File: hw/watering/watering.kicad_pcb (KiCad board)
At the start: 2 copper layers, 262 x 50 mm, 104 parts, among them J2 USB_C_Receptacle, J3 Conn_01x02_Pin, J4 Conn_01x02_Pin, J6 Conn_01x02_Pin, Q1 2N7002, SW2 KMS221GLFS, SW3 KMS221GLFS, U1 ESP32-C6, U10 MCP6002-xSN, U11 STI3508, U2 DRV8220DSG, U3 W25Q128JVS, U4 STI3508, U5 STI3508, U6 STI3508, U7 NCP163AFCT330T2G, U8 MCP6002-xSN, U9 MCP6002-xSN, Y1 40MHz, Y2 32768Hz

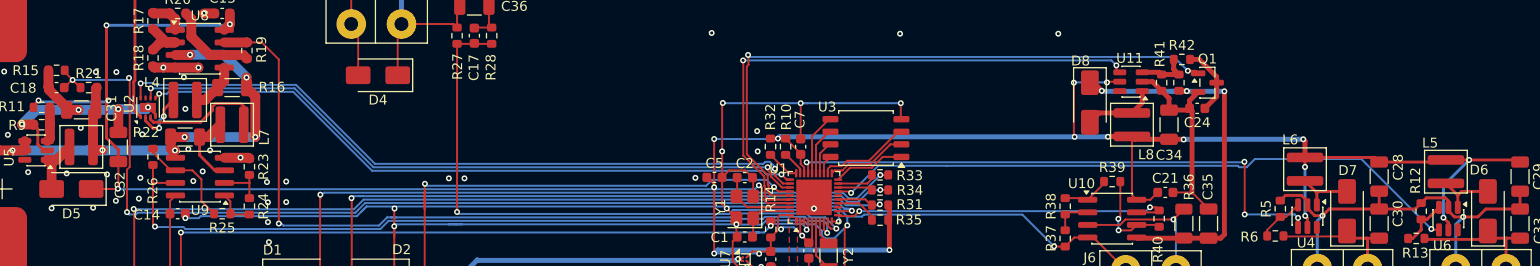
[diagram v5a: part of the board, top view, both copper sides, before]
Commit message: updated inductors
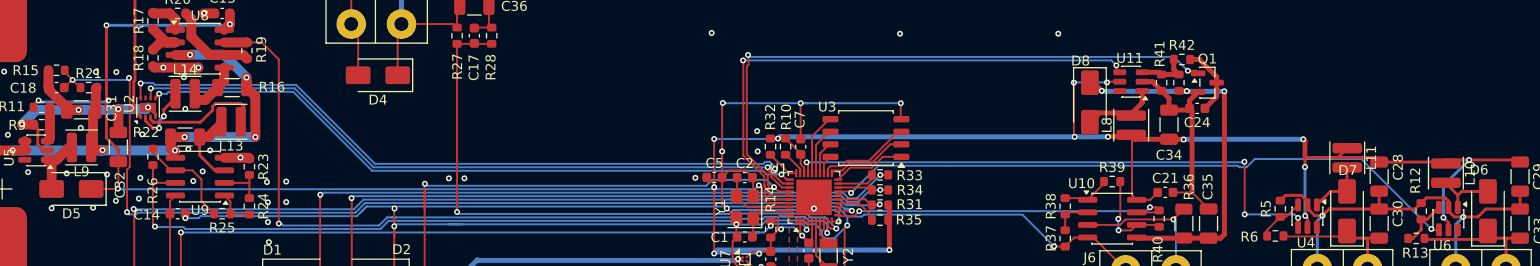
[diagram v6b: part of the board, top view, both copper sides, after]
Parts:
- removed L3, L4, L5, L6, L7: 22u, Inductor_SMD:L_Wuerth_MAPI-4030
- added L10: 22u, Inductor_SMD:L_Changjiang_FTC303020D, F.Cu at (252.0, 127.9)
- added L11: 22u, Inductor_SMD:L_Changjiang_FTC303020D, F.Cu at (242.0, 126.3)
- added L13: 22u, Inductor_SMD:L_Changjiang_FTC303020D, F.Cu at (129.2, 122.7)
- added L14: 22u, Inductor_SMD:L_Changjiang_FTC303020D, F.Cu at (124.5, 119.9)
- added L9: 22u, Inductor_SMD:L_Changjiang_FTC303020D, F.Cu at (114.0, 125.3)
- L8: footprint Inductor_SMD:L_Wuerth_MAPI-4030 -> Inductor_SMD:L_Changjiang_FTC303020D
- moved L8 0.09 mm to (220.2, 123.0)
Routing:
- net /+3V3: track 297.6 -> 299.3 mm

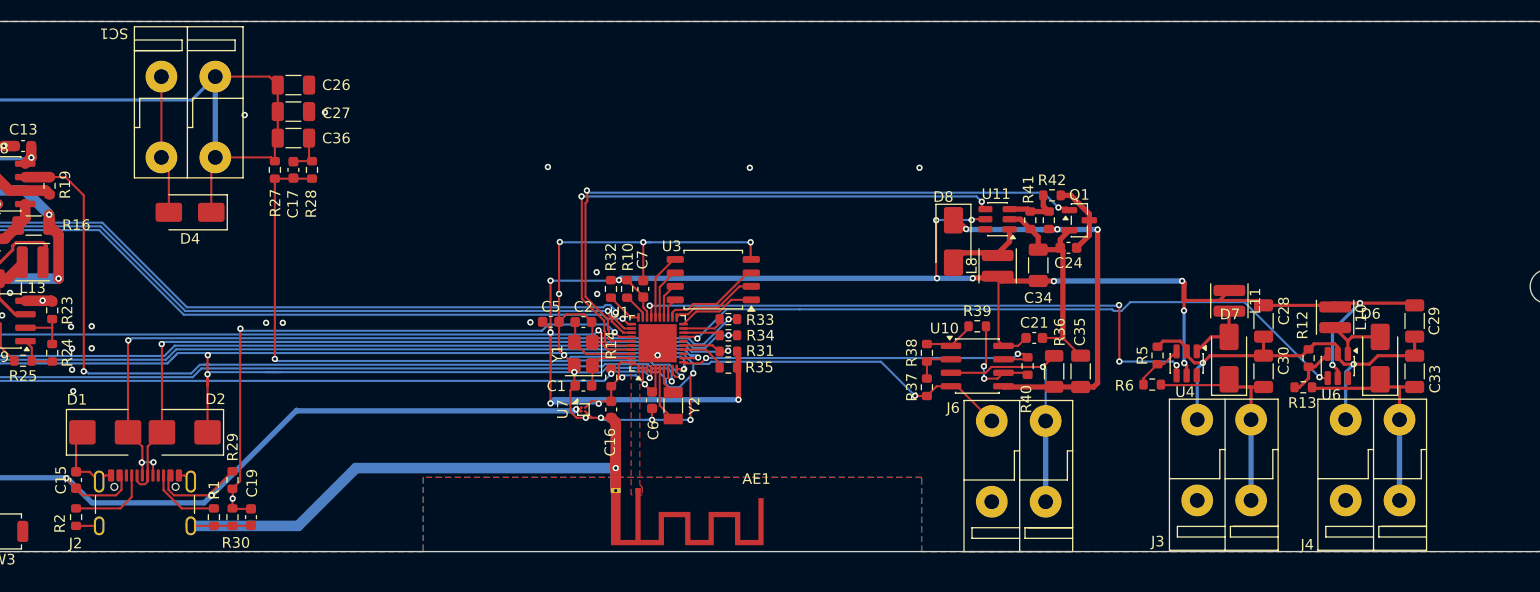
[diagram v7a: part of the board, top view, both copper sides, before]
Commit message: - updated bom - updated dorabo connector footprint - added some stitching vias
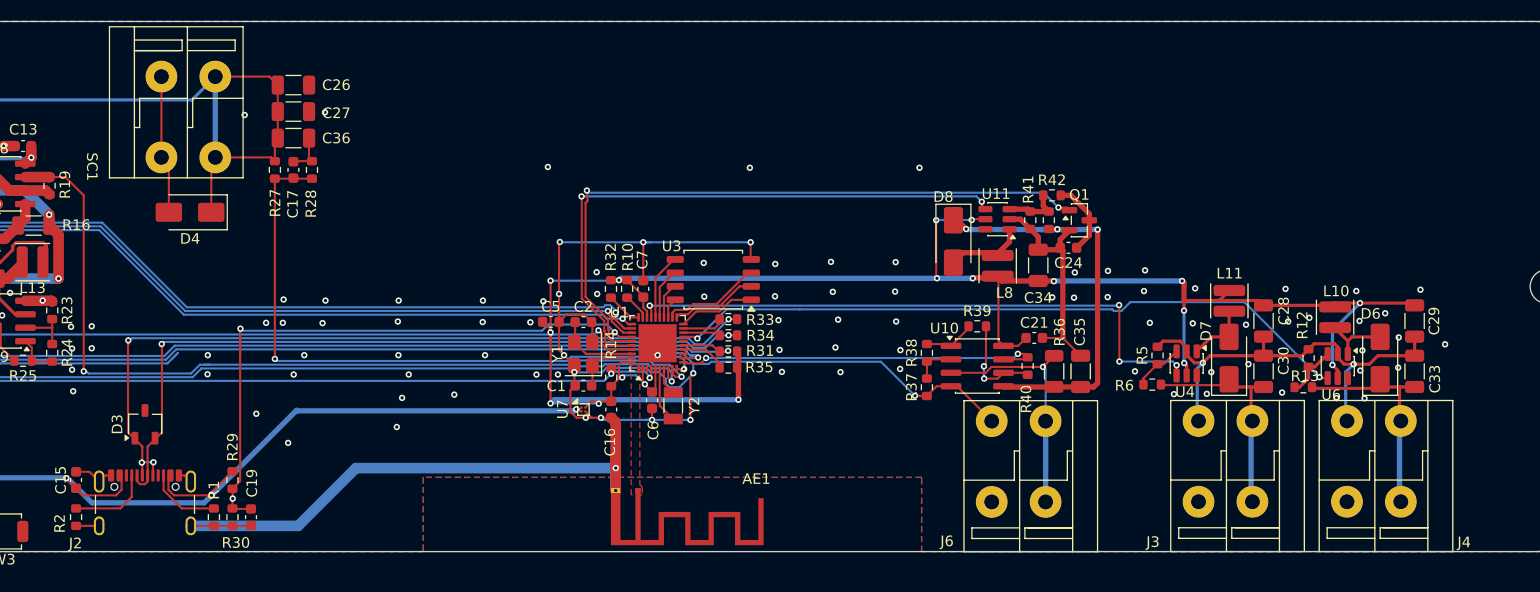
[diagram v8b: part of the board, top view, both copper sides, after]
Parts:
- removed D1, D2: SMBJ6.5CA, Diode_SMD:D_SMB
- added D3: D_TVS_Dual_AAC, Package_TO_SOT_SMD:TSOT-23, F.Cu at (139.8, 138.0)
- R1, R2: value 4k7 -> 5k1
- moved J3 0.18 mm to (241.5, 141.5)
- moved J4 0.18 mm to (255.5, 141.5)
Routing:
- net /GND: track 422.6 -> 329.4 mm, vias 59 -> 127
